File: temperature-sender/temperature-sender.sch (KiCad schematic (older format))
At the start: 43 parts, among them IC1 ATTINY2313A-S, K1 SERVO, P1 CONN_01X02, P2 CONN_01X02, P3 CONN_01X02, P6 ISP, P7 CONN_01X03, P8 CONN_01X03, SW1 SW_PUSH, SW2 SW_PUSH, U1 MCP1700T-3302E/TT, U2 TMP102, U3 78L09, U4 HT7550-1

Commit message: Some more changes, slowly getting there
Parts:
- removed C1, C6: 10uF, Capacitors_SMD:C_0603_HandSoldering, symbol CP
- removed P2, P3: CONN_01X02, kicad-footprints:Pin_Header_Angled_SMD_1x02, symbol CONN_01X02
- removed TP_PD3: TEST_POINT, kicad-footprints:TP_1mm, symbol TEST_POINT
- removed U1: MCP1700T-3302E/TT, Housings_SOT-23_SOT-143_TSOT-6:SOT-23_Handsoldering, symbol MCP1700T-3302E/TT
- removed U3: 78L09, Housings_TO-92:TO-92_Inline_Narrow_Oval, symbol 78XX
- removed U4: HT7550-1, Housings_SOT-89:SOT89-3_Housing_Handsoldering, symbol HT7550-1
- added C4, C5, C6, C7, C9: 10uF, Capacitors_SMD:C_0603_HandSoldering, symbol C
- added P4: CONN_01X04, kicad-footprints:Pin_Header_Angled_SMD_1x04, symbol CONN_01X04
- added R3: 240R, Resistors_SMD:R_0603_HandSoldering, symbol R
- added R4: 1k5, Resistors_SMD:R_0603_HandSoldering, symbol R
- added U1: AMS1117, kicad-footprints:SOT-223, symbol AMS1117
- added U2: LM317L, Housings_TO-92:TO-92_Inline_Narrow_Oval, symbol LM317L
- C2: value 1uF -> 10uF
- C8: renamed from C3; value C -> 10uF
- SW1: renamed from SW2; footprint Buttons_Switches_SMD:SW_SPST_PTS645 -> kicad-footprints:4x4x1.5mm_Tactile_Push_Button_SMD
- SW2: renamed from SW1; footprint Buttons_Switches_SMD:SW_SPST_PTS645 -> kicad-footprints:4x4x1.5mm_Tactile_Push_Button_SMD
- renumbered C4 to C1, C5 to C10, C7 to C3, D5 to D2, D2 to D4, D4 to D5, P6 to P1, P1 to P2, P7 to P3, P8 to P5, R6 to R1, R3 to R10, R4 to R5, R9 to R6, R5 to R7, R7 to R9, TP_PB0 to TP_PB1, TP_PB1 to TP_PB2, TP_PB4 to TP_PB3, TP_PD4 to TP_PD1, TP_PD5 to TP_PD2, TP_PD6 to TP_PD3, TP_XTAL2 to TP_XTAL1, TP_XTAL1 to TP_XTAL2, U2 to U3
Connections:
- net labels added: 9v, SERVO_SIG, SW, Vadj, Vin1, Vin2, Vin_rec
- net labels removed: +5V, +9V
- wire segments 110 -> 121
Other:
- note added: "Vout = 1.25*(1+R2/R1)\nVout = 1.25*(1+1500/240) \nVout = 9v"
- note removed: "TODO: Check pinning!!!."
- moved on the sheet: D3, R2

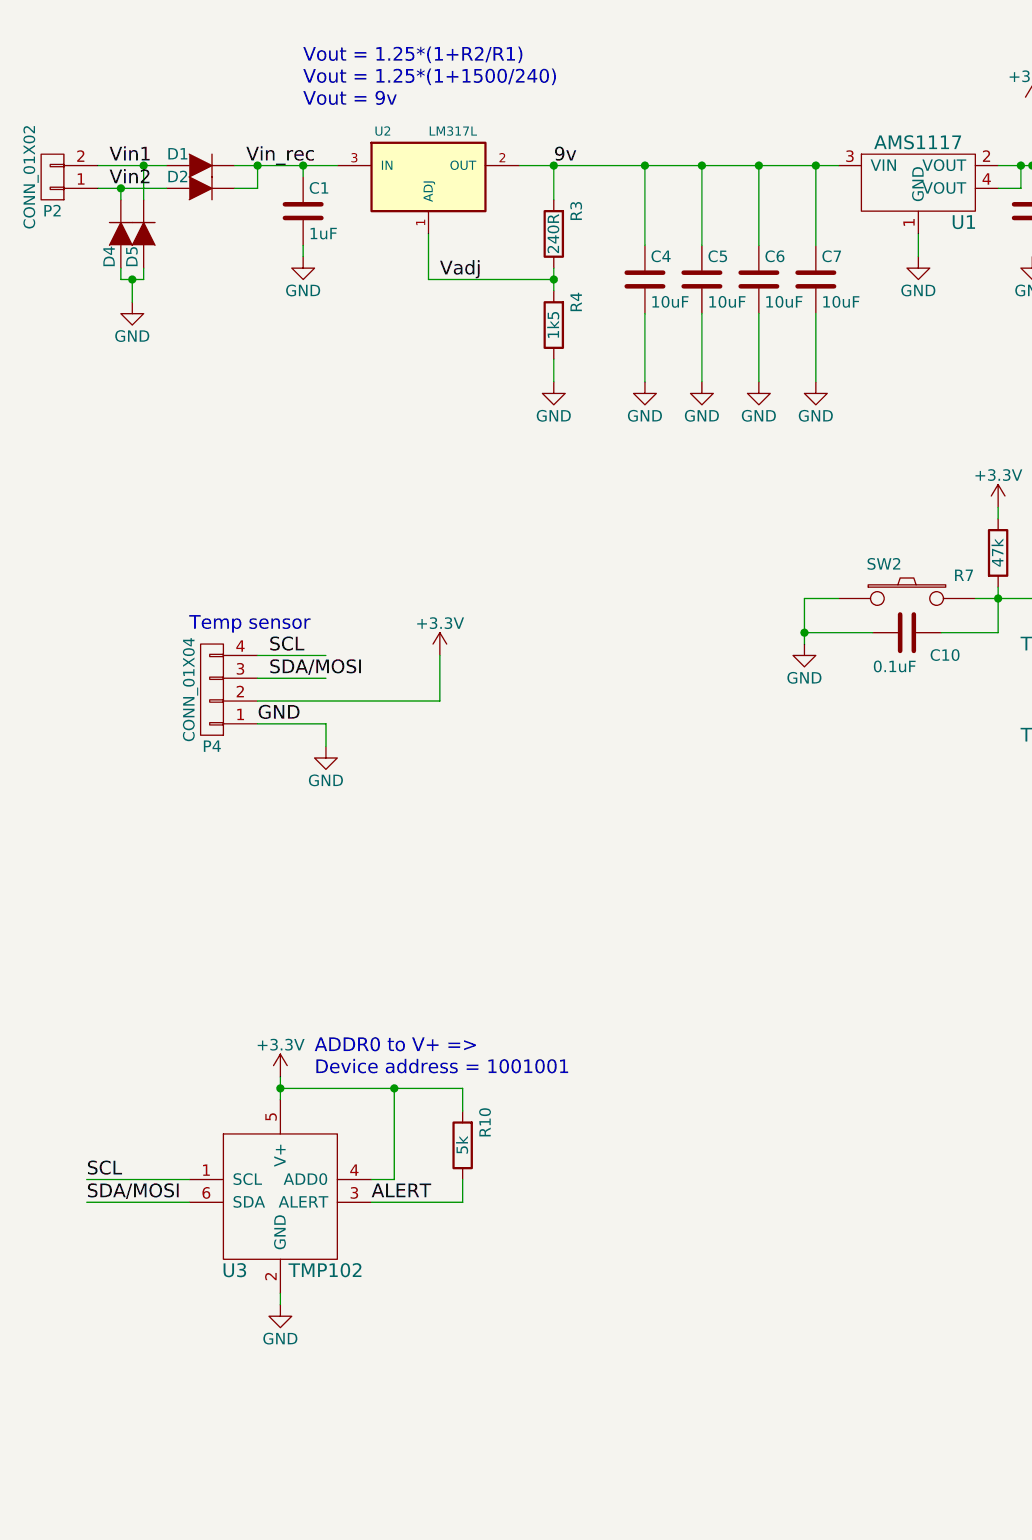
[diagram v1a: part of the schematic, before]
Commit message: Components placement mostly done
Problem with small temperature footprint. I like to have wider
power traces, but then it can't route this chip. Must figure out how
to solve it in KiCad.
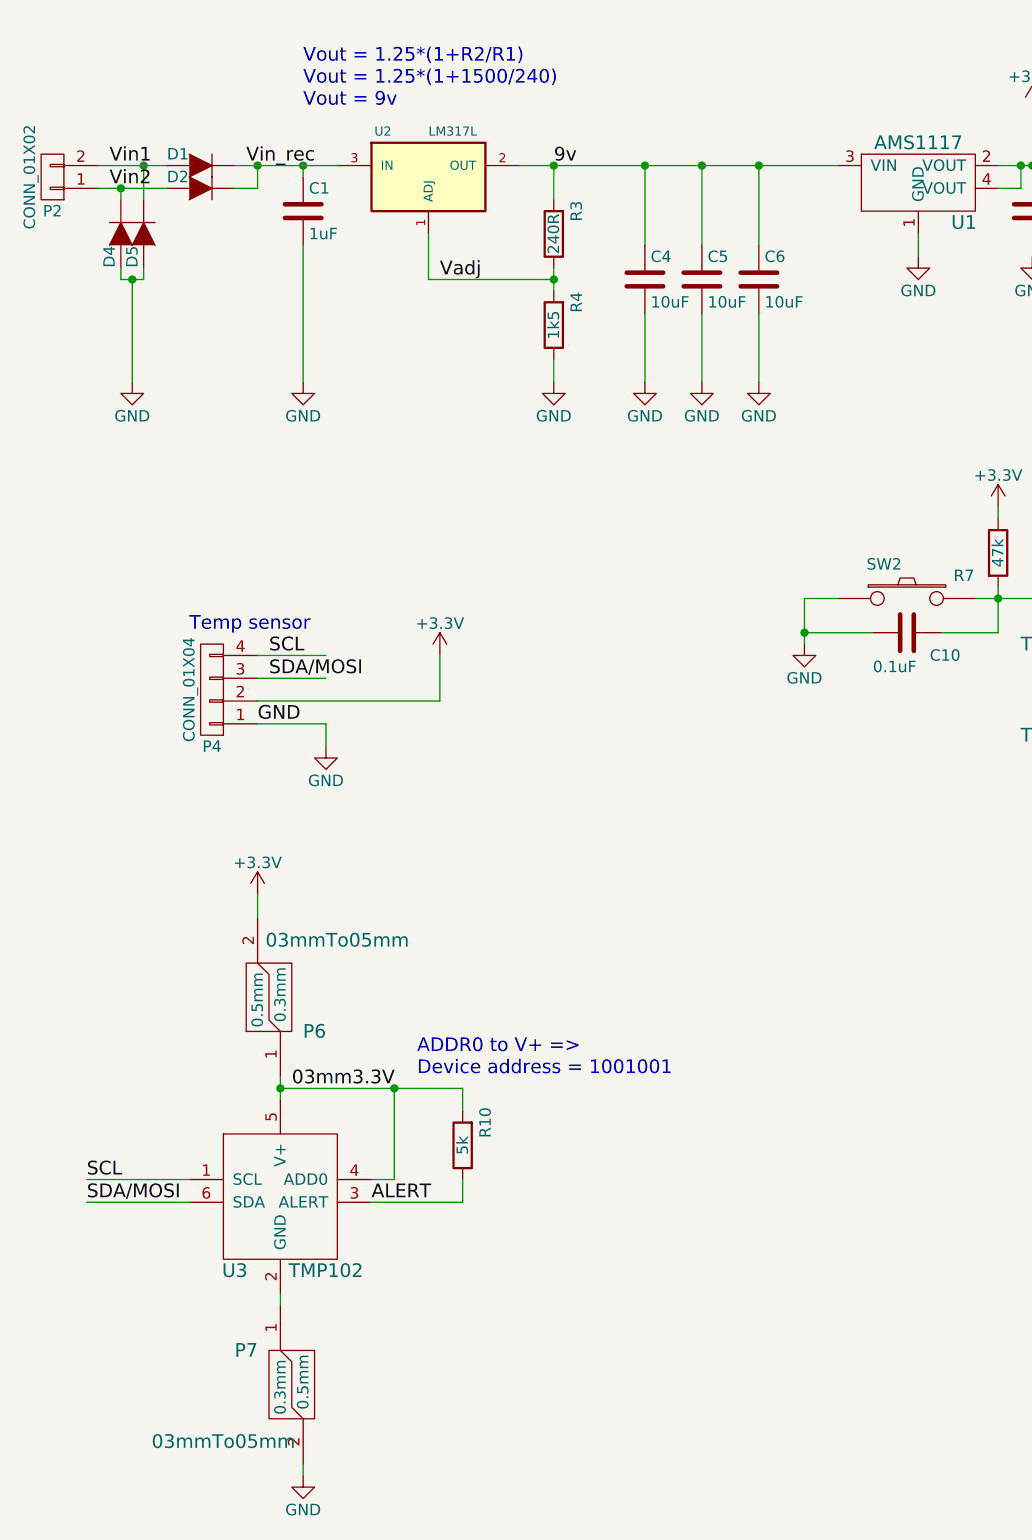
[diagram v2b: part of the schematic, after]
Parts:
- removed C7: 10uF, Capacitors_SMD:C_0603_HandSoldering, symbol C
- added P6, P7: 03mmTo05mm, kicad-footprints:03mmTo05mm, symbol 03mmTo05mm
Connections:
- net labels added: 03mm3.3V

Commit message: Temperature sender before import freerouting results
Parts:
- removed P4: CONN_01X04, kicad-footprints:Pin_Header_Angled_SMD_1x04, symbol CONN_01X04
- removed P6, P7: 03mmTo05mm, kicad-footprints:03mmTo05mm, symbol 03mmTo05mm
- removed TP_PB2: TEST_POINT, kicad-footprints:TP_1mm, symbol TEST_POINT
- removed U3: TMP102, kicad-footprints:SOT563, symbol TMP102
- added D6: Led_Small, LEDs:LED-0603, symbol Led_Small
- added GND1: TEST_POINT, Wire_Pads:SolderWirePad_single_1mmDrill, symbol TEST_POINT
- added P4: CONN_01X05, kicad-footprints:Pin_Header_Angled_SMD_1x05, symbol CONN_01X05
- R10: value 5k -> 330R
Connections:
- net labels removed: 03mm3.3V
- wire segments 121 -> 114
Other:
- note added: "Temp sensor connector"
- note removed: "ADDR0 to V+ =>\nDevice address = 1001001"
- note removed: "Temp sensor"
- moved on the sheet: D3, R2

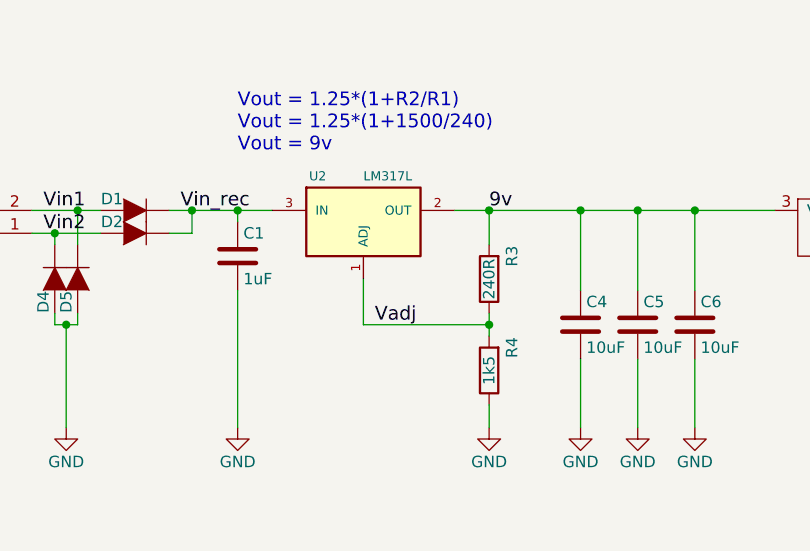
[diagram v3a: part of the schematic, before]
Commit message: Changed a couple of resistors on the temperature-sender
I did not have the exact values, so I changed to closest
match.
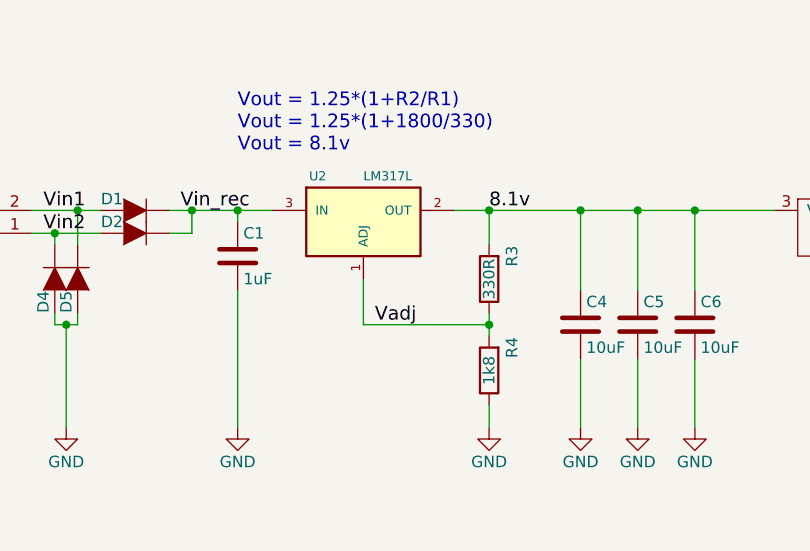
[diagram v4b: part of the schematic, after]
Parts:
- R3: value 240R -> 330R
- R4: value 1k5 -> 1k8
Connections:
- net labels added: 8.1v
- net labels removed: 9v
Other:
- note added: "Vout = 1.25*(1+R2/R1)\nVout = 1.25*(1+1800/330) \nVout = 8.1v"
- note removed: "Vout = 1.25*(1+R2/R1)\nVout = 1.25*(1+1500/240) \nVout = 9v"
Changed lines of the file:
@@
 P 2950 2200
 F 0 "R3" V 2850 2100 50  0000 C CNN
-F 1 "240R" V 2950 2200 50  0000 C CNN
+F 1 "330R" V 2950 2200 50  0000 C CNN
 F 2 "Resistors_SMD:R_0603_HandSoldering" V 2880 2200 30  0001 C CNN
 F 3 "" H 2950 2200 30  0000 C CNN
@@
 P 2950 2600
 F 0 "R4" V 2850 2500 50  0000 C CNN
-F 1 "1k5" V 2950 2600 50  0000 C CNN
+F 1 "1k8" V 2950 2600 50  0000 C CNN
 F 2 "Resistors_SMD:R_0603_HandSoldering" V 2880 2600 30  0001 C CNN
 F 3 "" H 2950 2600 30  0000 C CNN
@@
 $EndComp
 Text Notes 1850 1650 0    60   ~ 0
-Vout = 1.25*(1+R2/R1)\nVout = 1.25*(1+1500/240) \nVout = 9v
+Vout = 1.25*(1+R2/R1)\nVout = 1.25*(1+1800/330) \nVout = 8.1v
 $Comp
 L C C4
@@
 $EndComp
 Text Label 2950 1900 0    60   ~ 0
-9v
+8.1v
 $Comp
 L C C9
